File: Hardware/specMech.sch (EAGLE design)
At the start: 73 parts, among them IC1 MCP23008, J1 Molex 0022232081, J2 Molex 0022232081, J3 PINHD-1X8-MOLEX-SHROUD, J4 PINHD-1X8-MOLEX-SHROUD, J5 XPORT, J6 Molex 0022232081, J7 Molex 0022232081, J8 Molex 0022232081, U1 MCP23008-E/SO, U10 ADS1115, U2 MCP23008-E/SO, U3 TXB0102DCURVSSOP8, U4 MCP9808-E/MS, U5 TBD62083, U6 TBD62083SOP18-P-375-1.27, U7 MCP23008-E/SO, U8 MCP23008-E/SO, U9 ADS1115

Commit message: Worked on board layout
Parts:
- removed C1: 0.1uF, AUmlib:C-USC0805
- removed IC1: MCP23008, AUmlib:MCP23008MCP23008
- removed J1: Molex 0022232081, AUmlib:PINHD-1X8-MOLEX-SHROUD
- removed JP5: (no value), AUmlib:PINHD-1X2
- removed R1, R12, R17, R18, R19, R20, R21, R23, R24, R25, R26: 10K, AUmlib:R-US_R0805
- removed U6: TBD62083SOP18-P-375-1.27, AUmlib:TBD62083SOP18-P-375-1.27
- removed U7: MCP23008-E/SO, AUmlib:MCP23008-E/SO
- added C21: 0.1uF, AUmlib:C-USC0805
- added RN1, RN2: EXB-38V103JV, AUmlib:EXB-38V103JV
- added U11: MCP23008-E/SO, AUmlib:MCP23008-E/SO
- R15, R4: value 4K7 -> 10K
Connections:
- removed net /RST: IC1./RST, R17.2
- removed net AIN1: C14.1, R19.2, U9.AIN1
- removed net AIN2: C17.1, R24.2, U10.AIN1
- removed net INT: IC1.INT, R18.2
- removed net N$19: J1.5, U6.O4
- removed net N$23: J1.4, U6.O5
- removed net N$25: J1.3, U6.O6
- removed net N$26: J1.2, U6.O7
- removed net N$27: J1.1, U6.O8
- removed net N$28: U6.I8, U7.GP0
- removed net N$29: U6.I7, U7.GP1
- removed net N$30: U6.I6, U7.GP2
- removed net N$31: U6.I5, U7.GP3
- removed net N$32: U6.I4, U7.GP4
- removed net N$33: U6.I3, U7.GP5
- removed net N$34: U6.I2, U7.GP6
- removed net N$35: U6.I1, U7.GP7
- removed net N$58: R1.1, U7.!RESET
- removed net N$59: R12.1, U7.INT
- removed net N$6: J1.8, U6.O1
- removed net N$7: J1.7, U6.O2
- removed net N$8: J1.6, U6.O3
- removed net PUP: JP5.1, R15.2, R4.2
- new net A0B: J4.8, RN1.8
- new net A1B: J4.6, RN1.7
- new net A2B: J4.4, RN1.6
- new net A3B: J4.2, RN1.5
- new net N$69: C17.1, RN1.1, U10.AIN0
- new net N$70: R27.2, U10.ADDR, U10.AL/RDY
- new net N$71: J3.5, U11.GP4
- new net N$72: J3.7, U11.GP6
- net +12V: no longer U6.COM
- net +5V: now also C21.1, R4.1, U11.VDD; no longer C1.1, IC1.VCC, JP5.2, R1.2, R17.1, U7.VDD
- net A0A: now also RN2.8; no longer R21.1, R26.1
- net A1A: now also RN2.7; no longer R19.1, R24.1
- net A2A: now also RN2.6; no longer C20.1, J3.2, J3.4, J3.6, J3.8, R16.1, R23.2, U10.AIN2, U9.AIN2
- net A3A: now also J3.2, J3.4, J3.6, J3.8, R16.1, U9.AIN3; no longer R20.1, R25.1
- net GND: now also C21.2, J4.1, J4.3, J4.5, J4.7, R15.1, U11.A0, U11.A1, U11.A2, U11.VSS; no longer C1.2, IC1.A0, IC1.A1, IC1.A2, IC1.GND, R12.2, R18.1, U10.ADDR, U6.GND, U7.A0, U7.A1, U7.A2, U7.VSS
- net N$18: now also R15.2, U11.INT; no longer IC1.GP2, J3.5
- net N$5: now also R4.2, U11.!RESET; no longer IC1.GP0, J3.7
- net N$60: now also J3.1, U11.GP0; no longer IC1.GP4, J3.3
- net N$61: now also J3.3, U11.GP2; no longer IC1.GP6, J3.1
- net N$62: now also C16.1, RN2.1, U9.AIN0; no longer C15.1, R20.2, U9.AIN3
- net N$63: now also C15.1, RN2.2, U9.AIN1; no longer C16.1, R21.2, U9.AIN0
- net N$65: now also RN1.4, U10.AIN3; no longer R26.2, U10.AIN0
- net N$66: now also C14.1, RN2.3, U9.AIN2; no longer R27.2, U10.AL/RDY
- net N$67: now also RN1.3, U10.AIN2; no longer R25.2, U10.AIN3
- net N$68: now also C20.1, RN1.2, U10.AIN1; no longer R23.1
- net SCL: now also U11.SCL; no longer IC1.SCL, R15.1, U7.SCL
- net SDA: now also U11.SDA; no longer IC1.SDA, R4.1, U7.SDA
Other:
- note added: "ADC ADS1115 A3A for AD590 sensor"
- note removed: "ADC"
- note removed: "High Current Driver"
- note removed: "I2C Pullups"
- moved on the sheet: C10, C12, C13, C14, C15, C16, C17, C18, C19, C20, C9, J3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

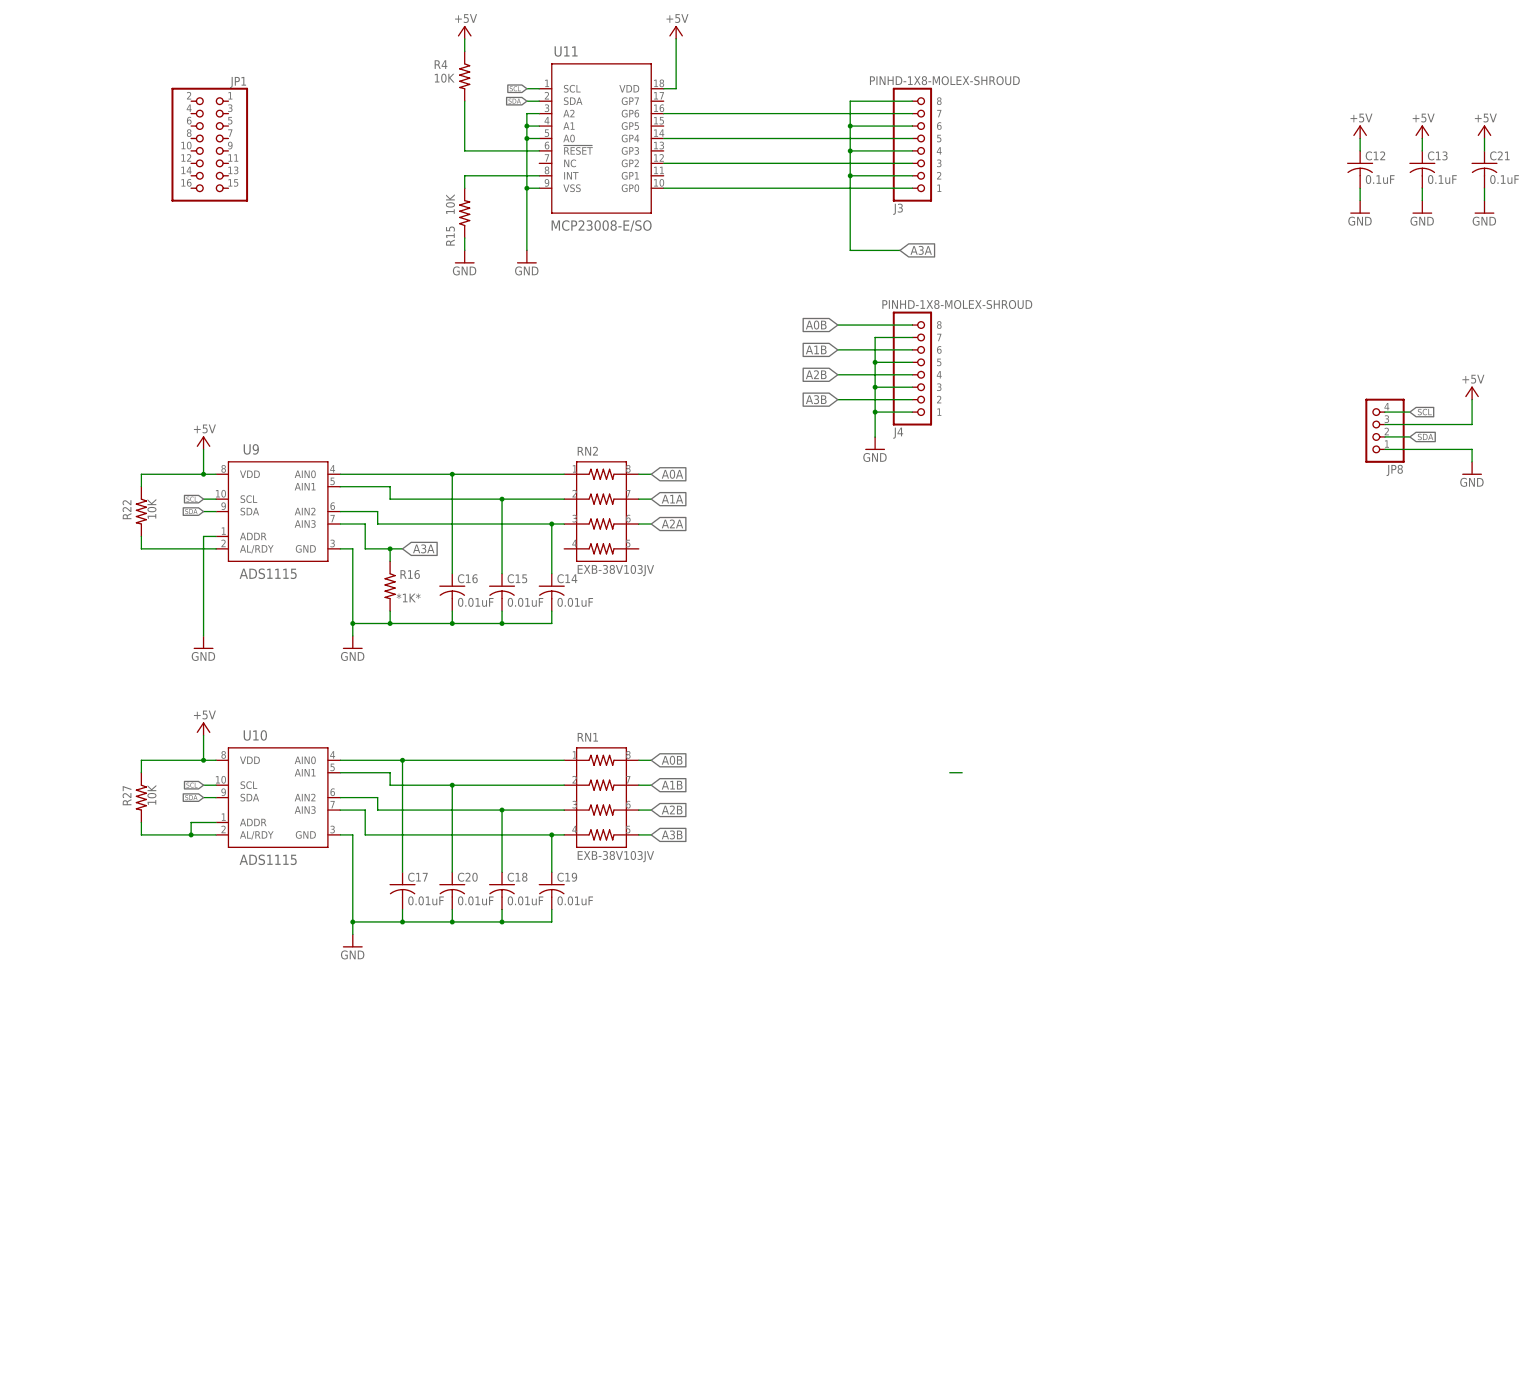
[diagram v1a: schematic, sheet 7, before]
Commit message: Remove backup Eagle files
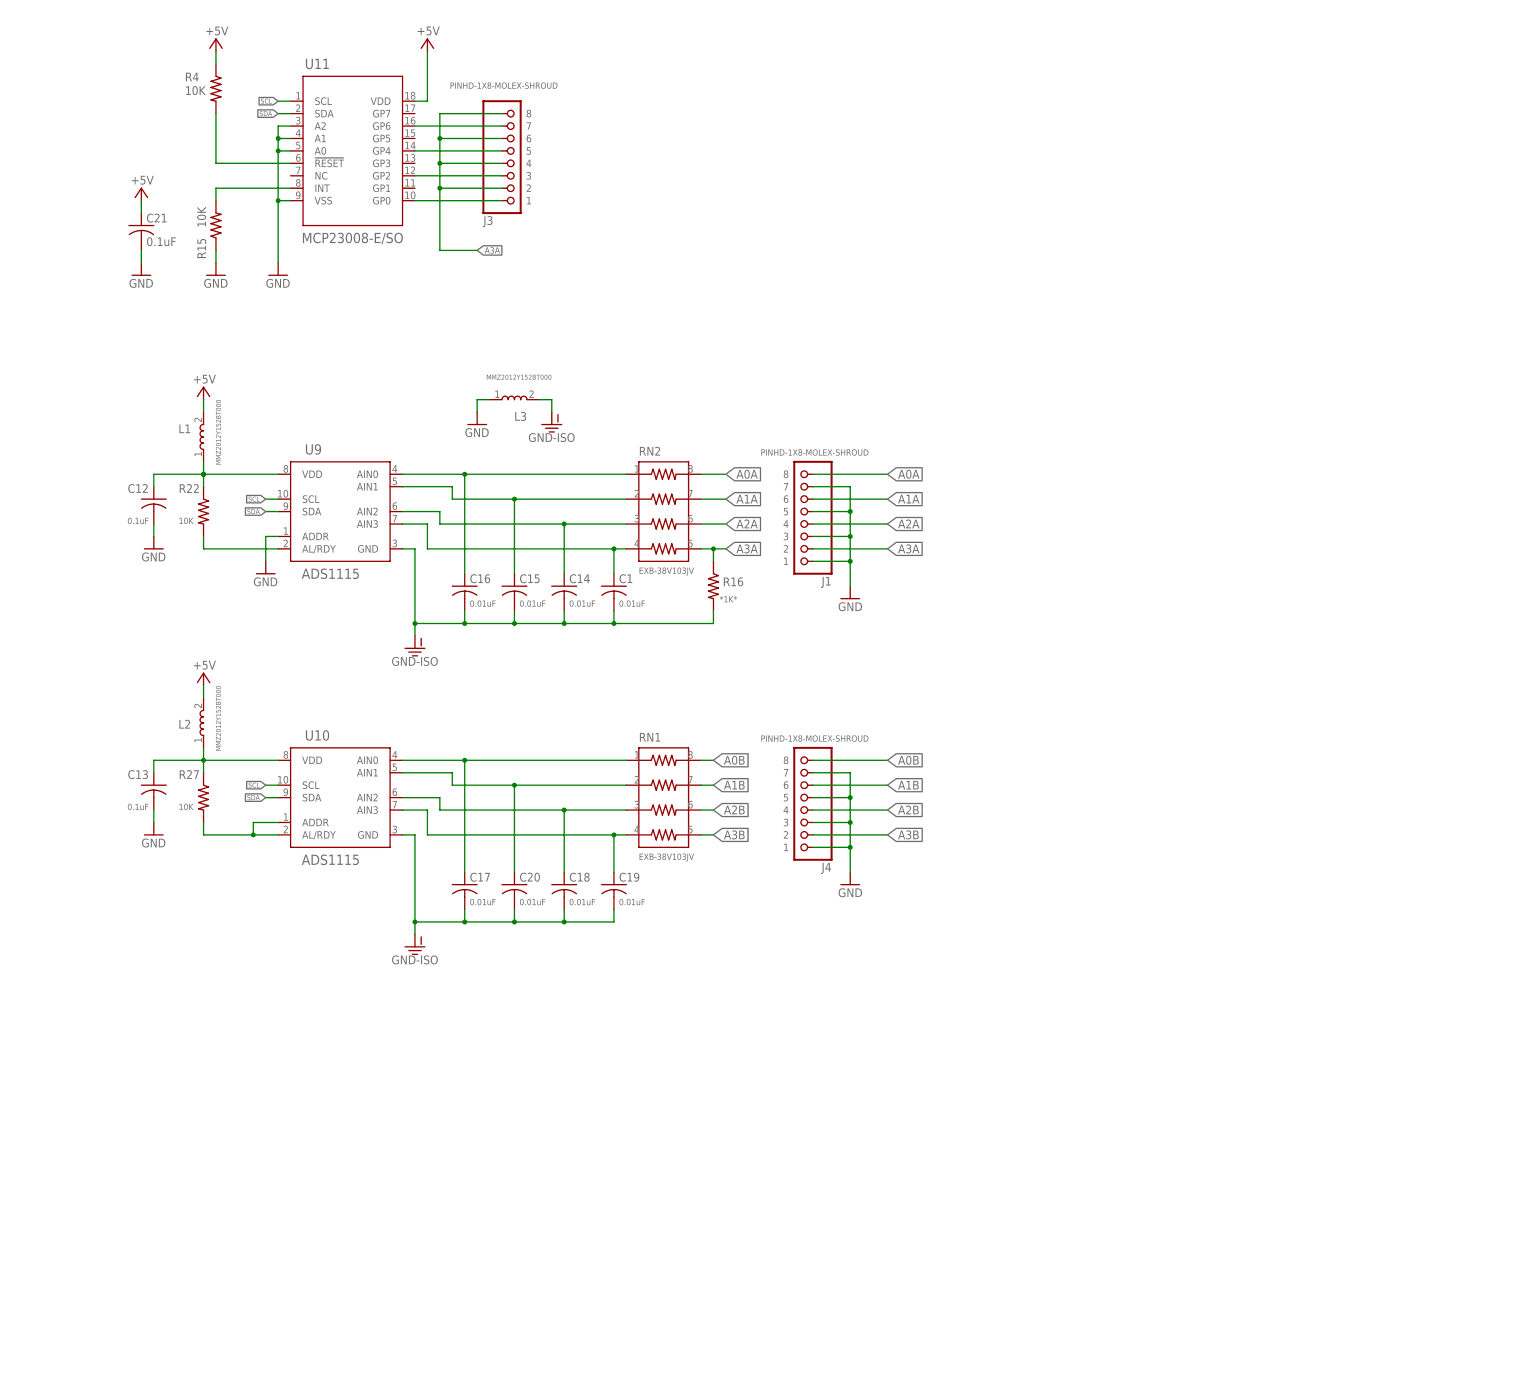
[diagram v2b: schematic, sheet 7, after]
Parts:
- removed JP1: (no value), AUmlib:PINHD-2X8
- removed JP8: (no value), AUmlib:PINHD-1X4/90
- removed VR1: OKI-78SR, AUmlib:OKI-78SR
- added C1: 0.01uF, AUmlib:C-USC0805
- added CNANO1: CURIOSITYNANO4809, AUmlib:CURIOSITYNANO4809
- added J1: PINHD-1X8-MOLEX-SHROUD, AUmlib:PINHD-1X8-MOLEX-SHROUD
- added L1, L2, L3: MMZ2012Y152BT000, AUmlib:MMZ2012Y152BT000
- added U6: OKI-78SR-5/1.5-W36E-C, AUmlib:OKI-78SR-5/1.5-W36E-C
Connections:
- new net GND-ISO: C1.2, C14.2, C15.2, C16.2, C17.2, C18.2, C19.2, C20.2, L3.2, R16.2, U10.GND, U9.GND
- new net N$6: C13.1, L2.1, R27.1, U10.VDD
- new net N$7: C12.1, L1.1, R22.1, U9.VDD
- net +12V: now also U6.VIN; no longer VR1.VIN
- net +5V: now also L1.2, L2.2, U6.VOUT; no longer C12.1, C13.1, JP8.3, R22.1, R27.1, U10.VDD, U9.VDD, VR1.VOUT
- net A0A: now also J1.8
- net A1A: now also J1.6
- net A2A: now also J1.4
- net A3A: now also C1.1, J1.2, RN2.4, RN2.5
- net GND: now also J1.1, J1.3, J1.5, J1.7, L3.1, U6.GND; no longer C14.2, C15.2, C16.2, C17.2, C18.2, C19.2, C20.2, JP8.1, R16.2, U10.GND, U9.GND, VR1.GND
- net SCL: no longer JP8.4
- net SDA: no longer JP8.2
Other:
- note added: "*1K* resistor is low TCR resistor ADS1115 VDD bypass cap should be MLCC type with low ESR & low ESL"
- note added: "A3A is the AD590 connection"
- note added: "AD590 selector"
- note added: "ADC ADS1115"
- note added: "High Current Driver Select"
- note added: "J4 on Z-World Board Pin 8 at 5.61, 1.73 in"
- note added: "J5 on Z-World Board Pin 8 at 5.61, 0.83 in"
- note added: "Power Header J2/J201 on the Z-World board Pin 8 is pin K on Z-World +12V at 5.61, 3.83 in"
- note removed: "*VALUE* indicates low TCR resistor Should filter other AIN pins & weak pullup pin 2 (AL/RDY) ADS1115 VDD bypass cap should be MLCC type with low ESR & low ESL"
- note removed: "AD590 + ADC"
- note removed: "ADC ADS1115 A3A for AD590 sensor"
- note removed: "ADC Inputs 1 for AD590 sensors 2 for humidity 2 for Ion Pump"
- note removed: "Analog Inputs"
- note removed: "Decoupling Caps"
- note removed: "J4 on Z-World Board Temp/RH here Pin 8 at 5.61, 1.73 in"
- note removed: "Port Expander"
- note removed: "Power & I2C Connection"
- note removed: "Power Header J2/J201 on the Z-World board Pin 8 us pin K on Z-World +12V at 5.61, 3.83 in"
- moved on the sheet: C11, C12, C13, C14, C15, C16, C17, C18, C19, C20, C21, J3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
